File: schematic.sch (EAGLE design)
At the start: 30 parts, among them Q1 SPB80P06P, Q2 IRF540, Q3 IRF4905

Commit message: Create connections
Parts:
- removed C5: (no value), rcl:C-EU025-025X050
- removed D3: 1A/50V/1.1V, SparkFun-DiscreteSemi:DIODE-PTH
- removed Q2: IRF540, transistor-power:IRF540
- added C1: 47uF, rcl:CPOL-EUE2.5-6
- added C100: (no value), rcl:C-EU025-025X050
- added D5: 1N5908, diode:1N5908
- added Q5: SPB80P06P, transistor-fet:SPB80P06P
- added R13: 100k, rcl:R-EU_0207/10
- C2: value (none) -> 1uF; device rcl:CPOL-EUE2.5-6 -> rcl:C-EU025-025X050
- C3, C4: value (none) -> 0.1uF
- D2: value 1N5908 -> 1A/50V/1.1V; device diode:1N5908 -> SparkFun-DiscreteSemi:DIODE-PTH
- Q1: value SPB80P06P -> IRF4905; device transistor-fet:SPB80P06P -> transistor-power:IRF4905
- Q3: value IRF4905 -> IRF540; device transistor-power:IRF4905 -> transistor-power:IRF540
- R1: value 100 -> 150
- R10: value (none) -> 10k
- R11: value (none) -> 100
- R12: value (none) -> 200k
- R2: value (none) -> 220
- R3: value (none) -> 820
- R4: value (none) -> 1k
- R5: value (none) -> 47k
- R6: value (none) -> 330
- R7: value (none) -> 0.1
- R9: value (none) -> 470
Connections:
- removed net N$2: LOAD.2, Q1.S
- removed net N$3: R4.1, R5.2
- new net N$10: D5.C, L1.1, Q1.D
- new net N$12: C100.2, R9.1, U$1.VCH
- new net N$13: Q1.G, Q3.S, R3.2, R6.1, R9.2
- new net N$14: C100.1, Q3.G, R3.1
- new net N$15: LED1.C, R4.1
- new net N$17: D2.C, R2.2
- new net N$19: C3.1, R1.1, U$1.VDD
- new net N$20: R5.2, U$1.RT
- new net N$23: C4.1, U$1.CBIAS, U$1.MODE
- new net N$25: D1.A, POWER.2, R1.2, R11.1, R8.2
- new net N$26: C1.+, C2.1, D1.C, D2.A, D4.C, LED1.A, LOAD.2, Q1.S, Q3.D, Q5.S, R6.2
- new net N$4: BATT.2, C4.2, R13.1, R5.1, R7.2, THM.2, U$1.CTG1, U$1.CTG2, U$1.SNS-, U$1.VSS1, U$1.VSS2
- new net N$5: R10.1, THM.1, U$1.THM
- new net N$6: R10.2, U$1.DIV
- new net N$7: R12.1, R13.2, U$1.VBATT
- new net N$8: BATT.1, D4.A, L1.2, Q5.D, R12.2, R2.1
- new net N$9: R4.2, U$1.LED1
- net GND: now also C1.-, C2.2, C3.2, D5.A, LOAD.1, R7.1, R8.1, U$1.SNS+
- net N$1: now also Q5.G, R11.2; no longer Q1.G, R1.2
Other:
- moved on the sheet: BATT, C3, C4, D1, D4, LED1, POWER, R1, R10, R11, R12, R2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

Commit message: Place elements a bit better
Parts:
- Q1: value IRF4905 -> (none); device transistor-power:IRF4905 -> transistor-power:PMOSFET_PTO220BV
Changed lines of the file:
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@@
 <part name="U$1" library="ic-ds2715-nimh-charger" deviceset="DS2715" device=""/>
 <part name="Q5" library="transistor-fet" library_urn="urn:adsk.eagle:library:396" deviceset="SPB80P06P" device=""/>
-<part name="Q1" library="transistor-power" library_urn="urn:adsk.eagle:library:400" deviceset="IRF4905" device=""/>
 <part name="Q3" library="transistor-power" library_urn="urn:adsk.eagle:library:400" deviceset="IRF540" device=""/>
 <part name="D5" library="diode" library_urn="urn:adsk.eagle:library:210" deviceset="1N5908" device=""/>
@@
 <part name="C100" library="rcl" library_urn="urn:adsk.eagle:library:334" deviceset="C-EU" device="025-025X050"/>
 <part name="R5" library="rcl" library_urn="urn:adsk.eagle:library:334" deviceset="R-EU_" device="0207/10" value="47k"/>
+<part name="Q1" library="transistor-power" library_urn="urn:adsk.eagle:library:400" deviceset="PMOSFET_P" device="TO220BV"/>
 </parts>
 <sheets>
@@
 <instance part="U$1" gate="G$1" x="35.56" y="68.58"/>
 <instance part="Q5" gate="G$1" x="2.54" y="127" rot="R90"/>
-<instance part="Q1" gate="G$1" x="53.34" y="111.76" rot="R90"/>
 <instance part="Q3" gate="G$1" x="20.32" y="109.22"/>
 <instance part="D5" gate="1" x="63.5" y="106.68" rot="R90"/>
@@
 <instance part="C100" gate="G$1" x="5.08" y="96.52"/>
 <instance part="R5" gate="G$1" x="10.16" y="76.2"/>
+<instance part="Q1" gate="G$1" x="53.34" y="111.76" rot="R90"/>
 </instances>
 <busses>
@@
 <net name="N$10" class="0">
 <segment>
-<pinref part="Q1" gate="G$1" pin="D"/>
 <pinref part="L1" gate="1" pin="1"/>
 <wire x1="58.42" y1="114.3" x2="63.5" y2="114.3" width="0.1524" layer="91"/>
@@
 <wire x1="63.5" y1="109.22" x2="63.5" y2="114.3" width="0.1524" layer="91"/>
 <junction x="63.5" y="114.3"/>
+<pinref part="Q1" gate="G$1" pin="D"/>
 </segment>
 </net>
@@
 <junction x="22.86" y="101.6"/>
 <pinref part="Q1" gate="G$1" pin="G"/>
-<wire x1="55.88" y1="106.68" x2="55.88" y2="101.6" width="0.1524" layer="91"/>
-<wire x1="55.88" y1="101.6" x2="40.64" y2="101.6" width="0.1524" layer="91"/>
+<wire x1="50.8" y1="106.68" x2="50.8" y2="101.6" width="0.1524" layer="91"/>
+<wire x1="50.8" y1="101.6" x2="40.64" y2="101.6" width="0.1524" layer="91"/>
 </segment>
 </net>
@@
 <wire x1="-40.64" y1="78.74" x2="-30.48" y2="78.74" width="0.1524" layer="91"/>
 <pinref part="R6" gate="G$1" pin="2"/>
-<pinref part="Q1" gate="G$1" pin="S"/>
 <wire x1="40.64" y1="114.3" x2="48.26" y2="114.3" width="0.1524" layer="91"/>
 <pinref part="Q3" gate="G$1" pin="D"/>
@@
 <junction x="-30.48" y="78.74"/>
 <junction x="-25.4" y="109.22"/>
-</segment>
-</net>
+<pinref part="Q1" gate="G$1" pin="S"/>
+</segment>
+</net>

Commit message: Improve placement of elements
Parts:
- D1, D5: value 1N5908 -> 1N5817-B; device diode:1N5908 -> diode:1N5817-B
- renumbered C100 to C5
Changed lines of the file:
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@@
 <part name="Q5" library="transistor-fet" library_urn="urn:adsk.eagle:library:396" deviceset="SPB80P06P" device=""/>
 <part name="Q3" library="transistor-power" library_urn="urn:adsk.eagle:library:400" deviceset="IRF540" device=""/>
-<part name="D5" library="diode" library_urn="urn:adsk.eagle:library:210" deviceset="1N5908" device=""/>
-<part name="D1" library="diode" library_urn="urn:adsk.eagle:library:210" deviceset="1N5908" device=""/>
 <part name="LOAD" library="SparkFun-Connectors" deviceset="CONN_02" device="POLAR"/>
 <part name="POWER" library="SparkFun-Connectors" deviceset="CONN_02" device="POLAR"/>
@@
 <part name="GND3" library="supply1" library_urn="urn:adsk.eagle:library:371" deviceset="GND" device=""/>
 <part name="GND4" library="supply1" library_urn="urn:adsk.eagle:library:371" deviceset="GND" device=""/>
-<part name="C100" library="rcl" library_urn="urn:adsk.eagle:library:334" deviceset="C-EU" device="025-025X050"/>
+<part name="C5" library="rcl" library_urn="urn:adsk.eagle:library:334" deviceset="C-EU" device="025-025X050"/>
 <part name="R5" library="rcl" library_urn="urn:adsk.eagle:library:334" deviceset="R-EU_" device="0207/10" value="47k"/>
 <part name="Q1" library="transistor-power" library_urn="urn:adsk.eagle:library:400" deviceset="PMOSFET_P" device="TO220BV"/>
+<part name="D1" library="diode" library_urn="urn:adsk.eagle:library:210" deviceset="1N581*" device="" technology="7-B"/>
+<part name="D5" library="diode" library_urn="urn:adsk.eagle:library:210" deviceset="1N581*" device="" technology="7-B"/>
 </parts>
 <sheets>
@@
 <instance part="Q5" gate="G$1" x="2.54" y="127" rot="R90"/>
 <instance part="Q3" gate="G$1" x="20.32" y="109.22"/>
-<instance part="D5" gate="1" x="63.5" y="106.68" rot="R90"/>
-<instance part="D1" gate="1" x="-35.56" y="109.22"/>
 <instance part="LOAD" gate="G$1" x="-15.24" y="139.7" rot="R270"/>
 <instance part="POWER" gate="G$1" x="-66.04" y="106.68"/>
@@
 <instance part="GND3" gate="1" x="-48.26" y="38.1"/>
 <instance part="GND4" gate="1" x="63.5" y="101.6"/>
-<instance part="C100" gate="G$1" x="5.08" y="96.52"/>
+<instance part="C5" gate="G$1" x="5.08" y="96.52"/>
 <instance part="R5" gate="G$1" x="10.16" y="76.2"/>
 <instance part="Q1" gate="G$1" x="53.34" y="111.76" rot="R90"/>
+<instance part="D1" gate="G$1" x="-35.56" y="109.22"/>
+<instance part="D5" gate="G$1" x="63.5" y="106.68" rot="R90"/>
 </instances>
 <busses>
@@
 <pinref part="LOAD" gate="G$1" pin="1"/>
 <pinref part="GND2" gate="1" pin="GND"/>
-</segment>
-<segment>
-<pinref part="D5" gate="1" pin="A"/>
-<pinref part="GND4" gate="1" pin="GND"/>
 </segment>
 <segment>
@@
 <pinref part="R8" gate="G$1" pin="1"/>
 <junction x="-45.72" y="40.64"/>
+</segment>
+<segment>
+<pinref part="GND4" gate="1" pin="GND"/>
+<pinref part="D5" gate="G$1" pin="A"/>
 </segment>
 </net>
@@
 <pinref part="L1" gate="1" pin="1"/>
 <wire x1="58.42" y1="114.3" x2="63.5" y2="114.3" width="0.1524" layer="91"/>
-<pinref part="D5" gate="1" pin="C"/>
 <wire x1="63.5" y1="114.3" x2="66.04" y2="114.3" width="0.1524" layer="91"/>
 <wire x1="63.5" y1="109.22" x2="63.5" y2="114.3" width="0.1524" layer="91"/>
 <junction x="63.5" y="114.3"/>
 <pinref part="Q1" gate="G$1" pin="D"/>
+<pinref part="D5" gate="G$1" pin="C"/>
 </segment>
 </net>
@@
 <wire x1="35.56" y1="88.9" x2="40.64" y2="88.9" width="0.1524" layer="91"/>
 <wire x1="40.64" y1="88.9" x2="40.64" y2="91.44" width="0.1524" layer="91"/>
-<pinref part="C100" gate="G$1" pin="2"/>
+<pinref part="C5" gate="G$1" pin="2"/>
 <wire x1="35.56" y1="88.9" x2="5.08" y2="88.9" width="0.1524" layer="91"/>
 <wire x1="5.08" y1="88.9" x2="5.08" y2="91.44" width="0.1524" layer="91"/>
@@
 <wire x1="5.08" y1="101.6" x2="5.08" y2="106.68" width="0.1524" layer="91"/>
 <wire x1="5.08" y1="106.68" x2="17.78" y2="106.68" width="0.1524" layer="91"/>
-<pinref part="C100" gate="G$1" pin="1"/>
+<pinref part="C5" gate="G$1" pin="1"/>
 <pinref part="R3" gate="G$1" pin="1"/>
 <wire x1="10.16" y1="101.6" x2="5.08" y2="101.6" width="0.1524" layer="91"/>
@@
 <wire x1="-45.72" y1="124.46" x2="-45.72" y2="109.22" width="0.1524" layer="91"/>
 <junction x="-20.32" y="124.46"/>
-<pinref part="D1" gate="1" pin="A"/>
 <wire x1="-45.72" y1="109.22" x2="-45.72" y2="50.8" width="0.1524" layer="91"/>
 <wire x1="-38.1" y1="109.22" x2="-45.72" y2="109.22" width="0.1524" layer="91"/>
@@
 <pinref part="POWER" gate="G$1" pin="2"/>
 <wire x1="-45.72" y1="109.22" x2="-58.42" y2="109.22" width="0.1524" layer="91"/>
+<pinref part="D1" gate="G$1" pin="A"/>
 </segment>
 </net>
@@
 <wire x1="-5.08" y1="109.22" x2="-12.7" y2="109.22" width="0.1524" layer="91"/>
 <junction x="-12.7" y="109.22"/>
-<pinref part="D1" gate="1" pin="C"/>
 <wire x1="-12.7" y1="109.22" x2="-25.4" y2="109.22" width="0.1524" layer="91"/>
 <pinref part="D2" gate="G$1" pin="A"/>
@@
 <junction x="-25.4" y="109.22"/>
 <pinref part="Q1" gate="G$1" pin="S"/>
-</segment>
-</net>
+<pinref part="D1" gate="G$1" pin="C"/>
+</segment>
+</net>

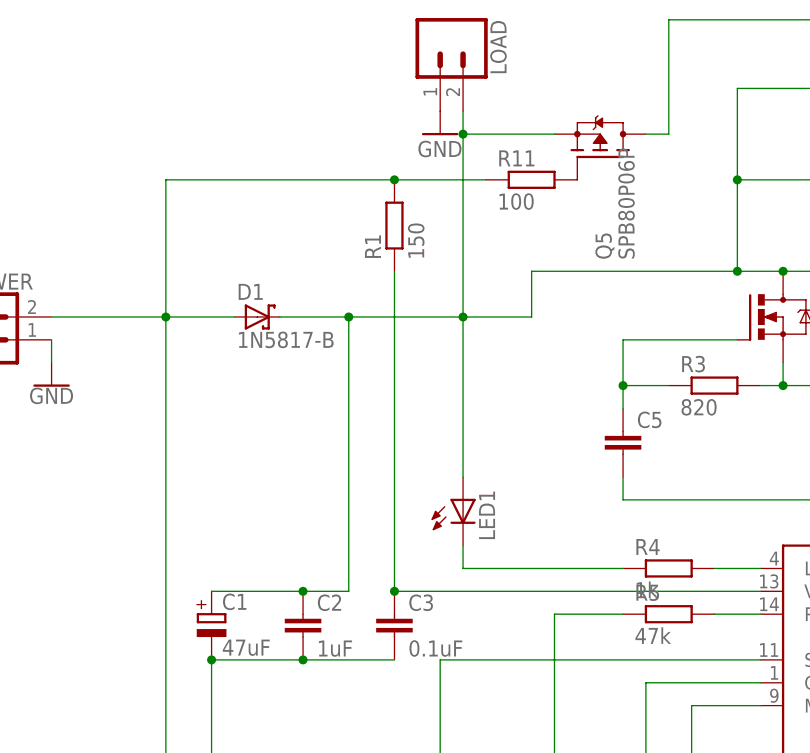
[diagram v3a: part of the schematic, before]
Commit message: start drawing the board
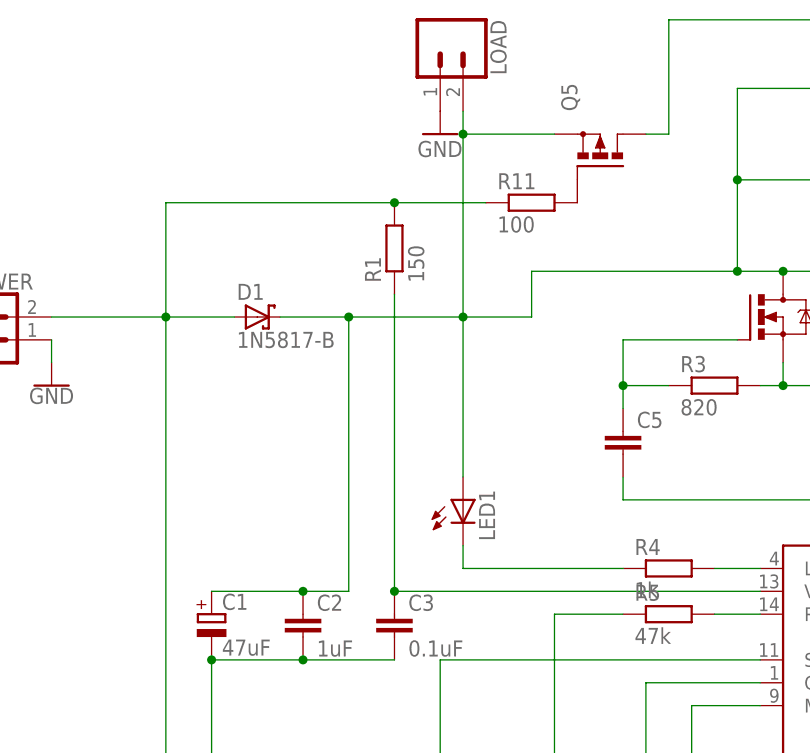
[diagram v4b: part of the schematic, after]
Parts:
- Q5: value SPB80P06P -> (none); device transistor-fet:SPB80P06P -> transistor-power:PMOSFET_PTO220BV
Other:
- moved on the sheet: R1, R11
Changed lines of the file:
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@@
 <parts>
 <part name="U$1" library="ic-ds2715-nimh-charger" deviceset="DS2715" device=""/>
-<part name="Q5" library="transistor-fet" library_urn="urn:adsk.eagle:library:396" deviceset="SPB80P06P" device=""/>
 <part name="Q3" library="transistor-power" library_urn="urn:adsk.eagle:library:400" deviceset="IRF540" device=""/>
 <part name="LOAD" library="SparkFun-Connectors" deviceset="CONN_02" device="POLAR"/>
@@
 <part name="D1" library="diode" library_urn="urn:adsk.eagle:library:210" deviceset="1N581*" device="" technology="7-B"/>
 <part name="D5" library="diode" library_urn="urn:adsk.eagle:library:210" deviceset="1N581*" device="" technology="7-B"/>
+<part name="Q5" library="transistor-power" library_urn="urn:adsk.eagle:library:400" deviceset="PMOSFET_P" device="TO220BV"/>
 </parts>
 <sheets>
@@
 <instances>
 <instance part="U$1" gate="G$1" x="35.56" y="68.58"/>
-<instance part="Q5" gate="G$1" x="2.54" y="127" rot="R90"/>
 <instance part="Q3" gate="G$1" x="20.32" y="109.22"/>
 <instance part="LOAD" gate="G$1" x="-15.24" y="139.7" rot="R270"/>
@@
 <instance part="LED1" gate="G$1" x="-12.7" y="88.9"/>
 <instance part="L1" gate="1" x="73.66" y="114.3"/>
-<instance part="R11" gate="G$1" x="-5.08" y="124.46"/>
+<instance part="R11" gate="G$1" x="-5.08" y="121.92"/>
 <instance part="GND1" gate="1" x="-58.42" y="101.6"/>
 <instance part="R2" gate="G$1" x="78.74" y="134.62" rot="R180"/>
-<instance part="R1" gate="G$1" x="-20.32" y="119.38" rot="R90"/>
+<instance part="R1" gate="G$1" x="-20.32" y="116.84" rot="R90"/>
 <instance part="R6" gate="G$1" x="40.64" y="109.22" rot="R90"/>
 <instance part="R9" gate="G$1" x="40.64" y="96.52" rot="R90"/>
@@
 <instance part="D1" gate="G$1" x="-35.56" y="109.22"/>
 <instance part="D5" gate="G$1" x="63.5" y="106.68" rot="R90"/>
+<instance part="Q5" gate="G$1" x="2.54" y="127" rot="R90"/>
 </instances>
 <busses>
@@
 <pinref part="GND4" gate="1" pin="GND"/>
 <pinref part="D5" gate="G$1" pin="A"/>
-</segment>
-</net>
-<net name="N$1" class="0">
-<segment>
-<pinref part="Q5" gate="G$1" pin="G"/>
-<pinref part="R11" gate="G$1" pin="2"/>
 </segment>
 </net>
@@
 <wire x1="99.06" y1="142.24" x2="10.16" y2="142.24" width="0.1524" layer="91"/>
 <wire x1="10.16" y1="142.24" x2="10.16" y2="129.54" width="0.1524" layer="91"/>
-<pinref part="Q5" gate="G$1" pin="D"/>
 <wire x1="10.16" y1="129.54" x2="7.62" y2="129.54" width="0.1524" layer="91"/>
 <pinref part="R12" gate="G$1" pin="2"/>
@@
 <wire x1="73.66" y1="124.46" x2="91.44" y2="124.46" width="0.1524" layer="91"/>
 <junction x="91.44" y="124.46"/>
+<pinref part="Q5" gate="G$1" pin="D"/>
 </segment>
 </net>
@@
 <pinref part="R1" gate="G$1" pin="1"/>
 <pinref part="C3" gate="G$1" pin="1"/>
-<wire x1="-20.32" y1="114.3" x2="-20.32" y2="78.74" width="0.1524" layer="91"/>
+<wire x1="-20.32" y1="111.76" x2="-20.32" y2="78.74" width="0.1524" layer="91"/>
 <pinref part="U$1" gate="G$1" pin="VDD"/>
 <wire x1="-20.32" y1="78.74" x2="20.32" y2="78.74" width="0.1524" layer="91"/>
@@
 <net name="N$25" class="0">
 <segment>
-<pinref part="R11" gate="G$1" pin="1"/>
 <pinref part="R1" gate="G$1" pin="2"/>
-<wire x1="-10.16" y1="124.46" x2="-20.32" y2="124.46" width="0.1524" layer="91"/>
 <pinref part="R8" gate="G$1" pin="2"/>
-<wire x1="-20.32" y1="124.46" x2="-45.72" y2="124.46" width="0.1524" layer="91"/>
-<wire x1="-45.72" y1="124.46" x2="-45.72" y2="109.22" width="0.1524" layer="91"/>
-<junction x="-20.32" y="124.46"/>
+<wire x1="-20.32" y1="121.92" x2="-45.72" y2="121.92" width="0.1524" layer="91"/>
+<wire x1="-45.72" y1="121.92" x2="-45.72" y2="109.22" width="0.1524" layer="91"/>
 <wire x1="-45.72" y1="109.22" x2="-45.72" y2="50.8" width="0.1524" layer="91"/>
 <wire x1="-38.1" y1="109.22" x2="-45.72" y2="109.22" width="0.1524" layer="91"/>
@@
 <wire x1="-45.72" y1="109.22" x2="-58.42" y2="109.22" width="0.1524" layer="91"/>
 <pinref part="D1" gate="G$1" pin="A"/>
+<pinref part="R11" gate="G$1" pin="1"/>
+<wire x1="-20.32" y1="121.92" x2="-10.16" y2="121.92" width="0.1524" layer="91"/>
+<junction x="-20.32" y="121.92"/>
 </segment>
 </net>
@@
 <pinref part="LOAD" gate="G$1" pin="2"/>
 <wire x1="-12.7" y1="132.08" x2="-12.7" y2="129.54" width="0.1524" layer="91"/>
-<pinref part="Q5" gate="G$1" pin="S"/>
 <wire x1="-12.7" y1="129.54" x2="-2.54" y2="129.54" width="0.1524" layer="91"/>
 <pinref part="LED1" gate="G$1" pin="A"/>
@@
 <pinref part="Q1" gate="G$1" pin="S"/>
 <pinref part="D1" gate="G$1" pin="C"/>
-</segment>
-</net>
+<pinref part="Q5" gate="G$1" pin="S"/>
+</segment>
+</net>
+<net name="N$1" class="0">
+<segment>
+<pinref part="Q5" gate="G$1" pin="G"/>
+<pinref part="R11" gate="G$1" pin="2"/>
+</segment>
+</net>

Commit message: Layout done
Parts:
- C5: value (none) -> 1nF
- R12: value 200k -> 500k
- R5: value 47k -> 160k
- R8: value (none) -> 100k
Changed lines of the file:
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@@
 <part name="R4" library="rcl" library_urn="urn:adsk.eagle:library:334" deviceset="R-EU_" device="0207/10" value="1k"/>
 <part name="R10" library="rcl" library_urn="urn:adsk.eagle:library:334" deviceset="R-EU_" device="0207/10" value="10k"/>
-<part name="R12" library="rcl" library_urn="urn:adsk.eagle:library:334" deviceset="R-EU_" device="0207/10" value="200k"/>
+<part name="R12" library="rcl" library_urn="urn:adsk.eagle:library:334" deviceset="R-EU_" device="0207/10" value="500k"/>
 <part name="R13" library="rcl" library_urn="urn:adsk.eagle:library:334" deviceset="R-EU_" device="0207/10" value="100k"/>
 <part name="R7" library="rcl" library_urn="urn:adsk.eagle:library:334" deviceset="R-EU_" device="0207/10" value="0.1"/>
-<part name="R8" library="rcl" library_urn="urn:adsk.eagle:library:334" deviceset="R-EU_" device="0207/10"/>
+<part name="R8" library="rcl" library_urn="urn:adsk.eagle:library:334" deviceset="R-EU_" device="0207/10" value="100k"/>
 <part name="C2" library="rcl" library_urn="urn:adsk.eagle:library:334" deviceset="C-EU" device="025-025X050" value="1uF"/>
 <part name="C3" library="rcl" library_urn="urn:adsk.eagle:library:334" deviceset="C-EU" device="025-025X050" value="0.1uF"/>
@@
 <part name="GND3" library="supply1" library_urn="urn:adsk.eagle:library:371" deviceset="GND" device=""/>
 <part name="GND4" library="supply1" library_urn="urn:adsk.eagle:library:371" deviceset="GND" device=""/>
-<part name="C5" library="rcl" library_urn="urn:adsk.eagle:library:334" deviceset="C-EU" device="025-025X050"/>
-<part name="R5" library="rcl" library_urn="urn:adsk.eagle:library:334" deviceset="R-EU_" device="0207/10" value="47k"/>
+<part name="C5" library="rcl" library_urn="urn:adsk.eagle:library:334" deviceset="C-EU" device="025-025X050" value="1nF"/>
+<part name="R5" library="rcl" library_urn="urn:adsk.eagle:library:334" deviceset="R-EU_" device="0207/10" value="160k"/>
 <part name="Q1" library="transistor-power" library_urn="urn:adsk.eagle:library:400" deviceset="PMOSFET_P" device="TO220BV"/>
 <part name="D1" library="diode" library_urn="urn:adsk.eagle:library:210" deviceset="1N581*" device="" technology="7-B"/>
